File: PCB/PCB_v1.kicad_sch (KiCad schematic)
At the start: 9 parts, among them J1 Accelerometer, J2 Flysky FS2A Receiver, J3 DC-DC, J4 Battery Left, J5 Battery Right, J6 ESC Left, J7 ESC Right, J8 LED, U1 Teensy4.0

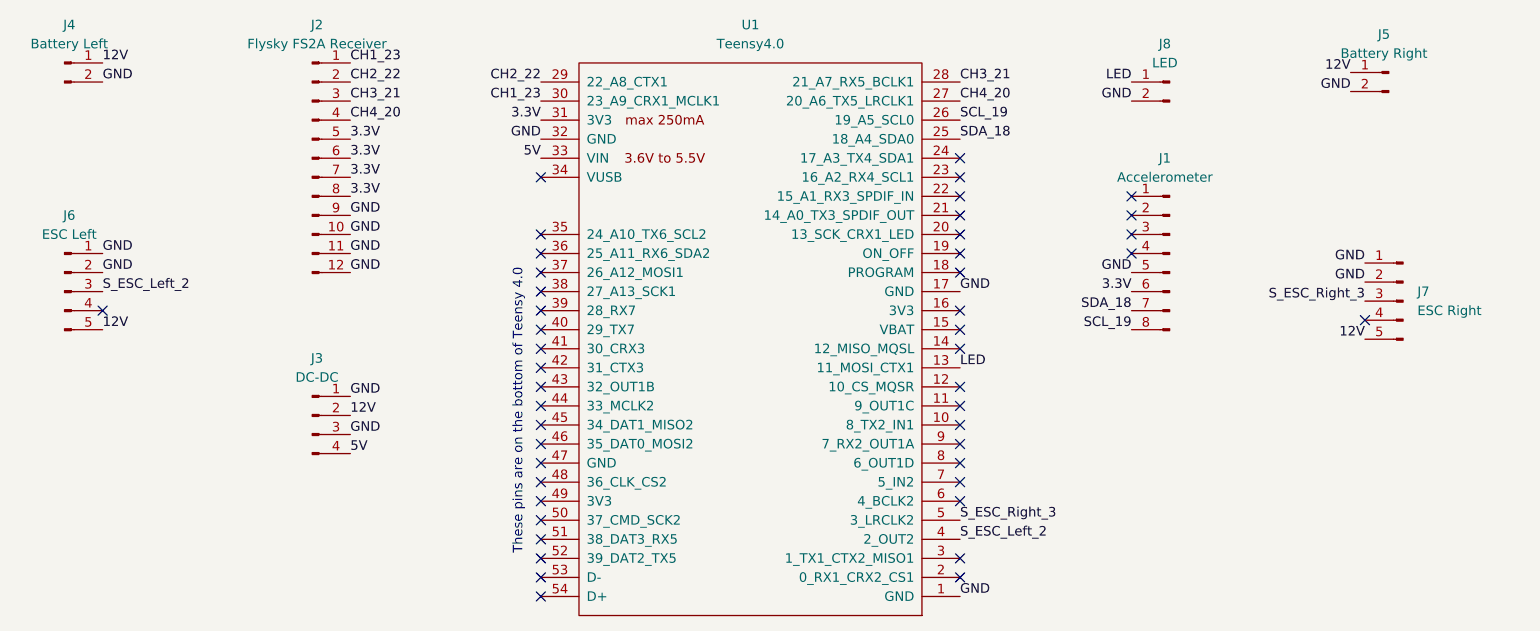
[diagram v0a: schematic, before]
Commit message: Put components onto PCB
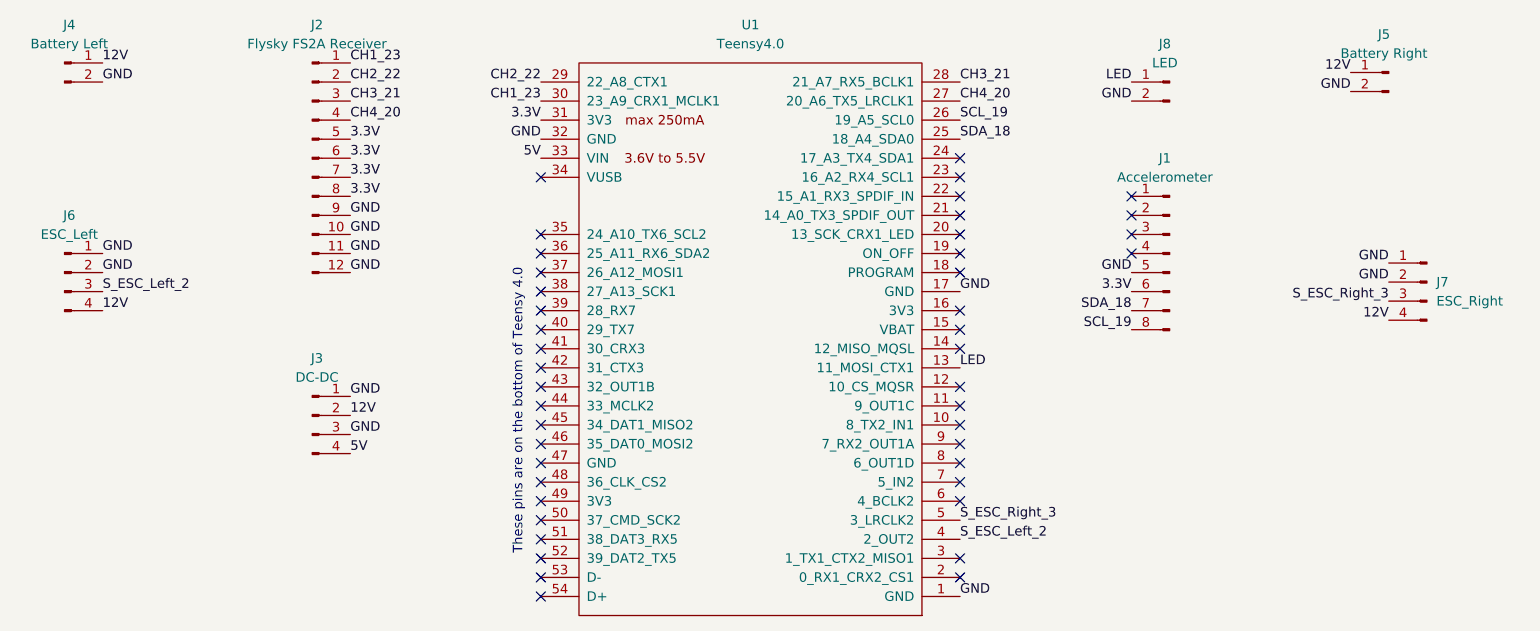
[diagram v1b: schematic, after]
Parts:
- removed J6: ESC Left, Stuffed Crust:ESC, symbol Connector:Conn_01x05_Pin
- removed J7: ESC Right, Stuffed Crust:ESC, symbol Connector:Conn_01x05_Pin
- added J6: ESC_Left, Stuffed Crust:ESC, symbol Connector:Conn_01x04_Pin
- added J7: ESC_Right, Stuffed Crust:ESC, symbol Connector:Conn_01x04_Pin
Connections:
- net 12V: now also J6.4 (Pin_4), J7.4 (Pin_4)
- net GND: now also J6.1 (Pin_1), J6.2 (Pin_2), J7.1 (Pin_1), J7.2 (Pin_2)
- net S_ESC_Left_2: now also J6.3 (Pin_3)
- net S_ESC_Right_3: now also J7.3 (Pin_3)
- no-connect marks 46 -> 44
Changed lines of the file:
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@@
-	)
-	(no_connect
-		(at 63.5 96.52)
 	)
 	(no_connect
@@
 	(no_connect
 		(at 200.66 83.82)
-	)
-	(no_connect
-		(at 231.775 97.79)
 	)
 	(no_connect
@@
 	)
 	(label "12V"
-		(at 231.775 100.33 180)
+		(at 234.95 97.79 180)
 		(effects
 			(font
@@
 	)
 	(label "GND"
-		(at 231.775 90.17 180)
+		(at 234.95 90.17 180)
 		(effects
 			(font
@@
 	)
 	(label "S_ESC_Right_3"
-		(at 231.775 95.25 180)
+		(at 234.95 95.25 180)
 		(effects
 			(font
@@
 	)
 	(label "GND"
-		(at 231.775 92.71 180)
+		(at 234.95 92.71 180)
 		(effects
 			(font
@@
 	)
 	(label "12V"
-		(at 63.5 99.06 0)
+		(at 63.5 96.52 0)
 		(effects
 			(font
@@
 			)
 			(justify left bottom)
-		)
-	)
-	(symbol
-		(lib_id "Connector:Conn_01x05_Pin")
-		(at 58.42 93.98 0)
-		(unit 1)
-		(exclude_from_sim no)
-		(in_bom yes)
-		(on_board yes)
-		(dnp no)
-		(fields_autoplaced yes)
-		(property "Reference" "J6"
-			(at 59.055 83.82 0)
-			(effects
-				(font
-					(size 1.27 1.27)
-				)
-			)
-		)
-		(property "Value" "ESC Left"
-			(at 59.055 86.36 0)
-			(effects
-				(font
-					(size 1.27 1.27)
-				)
-			)
-		)
-		(property "Footprint" "Stuffed Crust:ESC"
-			(at 58.42 93.98 0)
-			(effects
-				(font
-					(size 1.27 1.27)
-				)
-				(hide yes)
-			)
-		)
-		(property "Datasheet" "~"
-			(at 58.42 93.98 0)
-			(effects
-				(font
-					(size 1.27 1.27)
-				)
-				(hide yes)
-			)
-		)
-		(property "Description" "Generic connector, single row, 01x05, script generated"
-			(at 58.42 93.98 0)
-			(effects
-				(font
-					(size 1.27 1.27)
-				)
-				(hide yes)
-			)
-		)
-		(pin "1"
-		)
-		(pin "2"
-		)
-		(pin "3"
-		)
-		(pin "4"
-		)
-		(pin "5"
-		)
-		(instances
-			(project ""
-				(path "/be294340-84e5-4c43-afbb-c0b6a21202d8"
-					(reference "J6")
-					(unit 1)
-				)
-			)
-		)
-	)
-	(symbol
-		(lib_id "Connector:Conn_01x05_Pin")
-		(at 236.855 95.25 0)
-		(mirror y)
-		(unit 1)
-		(exclude_from_sim no)
-		(in_bom yes)
-		(on_board yes)
-		(dnp no)
-		(fields_autoplaced yes)
-		(property "Reference" "J7"
-			(at 238.76 93.9799 0)
-			(effects
-				(font
-					(size 1.27 1.27)
-				)
-				(justify right)
-			)
-		)
-		(property "Value" "ESC Right"
-			(at 238.76 96.5199 0)
-			(effects
-				(font
-					(size 1.27 1.27)
-				)
-				(justify right)
-			)
-		)
-		(property "Footprint" "Stuffed Crust:ESC"
-			(at 236.855 95.25 0)
-			(effects
-				(font
-					(size 1.27 1.27)
-				)
-				(hide yes)
-			)
-		)
-		(property "Datasheet" "~"
-			(at 236.855 95.25 0)
-			(effects
-				(font
-					(size 1.27 1.27)
-				)
-				(hide yes)
-			)
-		)
-		(property "Description" "Generic connector, single row, 01x05, script generated"
-			(at 236.855 95.25 0)
-			(effects
-				(font
-					(size 1.27 1.27)
-				)
-				(hide yes)
-			)
-		)
-		(pin "1"
-		)
-		(pin "2"
-		)
-		(pin "3"
-		)
-		(pin "4"
-		)
-		(pin "5"
-		)
-		(instances
-			(project "PCB_v1"
-				(path "/be294340-84e5-4c43-afbb-c0b6a21202d8"
-					(reference "J7")
-					(unit 1)
-				)
-			)
 		)
 	)
@@
 	)
 	(symbol
+		(lib_id "Connector:Conn_01x04_Pin")
+		(at 240.03 92.71 0)
+		(mirror y)
+		(unit 1)
+		(exclude_from_sim no)
+		(in_bom yes)
+		(on_board yes)
+		(dnp no)
+		(fields_autoplaced yes)
+		(property "Reference" "J7"
+			(at 241.3 92.7099 0)
+			(effects
+				(font
+					(size 1.27 1.27)
+				)
+				(justify right)
+			)
+		)
+		(property "Value" "ESC_Right"
+			(at 241.3 95.2499 0)
+			(effects
+				(font
+					(size 1.27 1.27)
+				)
+				(justify right)
+			)
+		)
+		(property "Footprint" "Stuffed Crust:ESC"
+			(at 240.03 92.71 0)
+			(effects
+				(font
+					(size 1.27 1.27)
+				)
+				(hide yes)
+			)
+		)
+		(property "Datasheet" "~"
+			(at 240.03 92.71 0)
+			(effects
+				(font
+					(size 1.27 1.27)
+				)
+				(hide yes)
+			)
+		)
+		(property "Description" "Generic connector, single row, 01x04, script generated"
+			(at 240.03 92.71 0)
+			(effects
+				(font
+					(size 1.27 1.27)
+				)
+				(hide yes)
+			)
+		)
+		(pin "3"
+		)
+		(pin "4"
+		)
+		(pin "1"
+		)
+		(pin "2"
+		)
+		(instances
+			(project ""
+				(path "/be294340-84e5-4c43-afbb-c0b6a21202d8"
+					(reference "J7")
+					(unit 1)
+				)
+			)
+		)
+	)
+	(symbol
 		(lib_id "Connector:Conn_01x02_Pin")
 		(at 234.95 64.77 0)
@@
 					(unit 1)
 				)
+			)
+		)
+	)
+	(symbol
+		(lib_id "Connector:Conn_01x04_Pin")
+		(at 58.42 91.44 0)
+		(unit 1)
+		(exclude_from_sim no)
+		(in_bom yes)
+		(on_board yes)
+		(dnp no)
+		(fields_autoplaced yes)
+		(property "Reference" "J6"
+			(at 59.055 83.82 0)
+			(effects
+				(font
+					(size 1.27 1.27)
+				)
+			)
+		)
+		(property "Value" "ESC_Left"
+			(at 59.055 86.36 0)
+			(effects
+				(font
+					(size 1.27 1.27)
+				)
+			)
+		)
+		(property "Footprint" "Stuffed Crust:ESC"
+			(at 58.42 91.44 0)
+			(effects
+				(font
+					(size 1.27 1.27)
+				)
+				(hide yes)
+			)
+		)
+		(property "Datasheet" "~"
+			(at 58.42 91.44 0)
+			(effects
+				(font
+					(size 1.27 1.27)
+				)
+				(hide yes)
+			)
+		)
+		(property "Description" "Generic connector, single row, 01x04, script generated"
+			(at 58.42 91.44 0)
+			(effects
+				(font
+					(size 1.27 1.27)
+				)
+				(hide yes)
+			)
+		)
+		(pin "4"
+		)
+		(pin "3"
+		)
+		(pin "2"
+		)
+		(pin "1"
+		)
+		(instances
+			(project ""
+				(path "/be294340-84e5-4c43-afbb-c0b6a21202d8"
+					(reference "J6")
+					(unit 1)
+				)

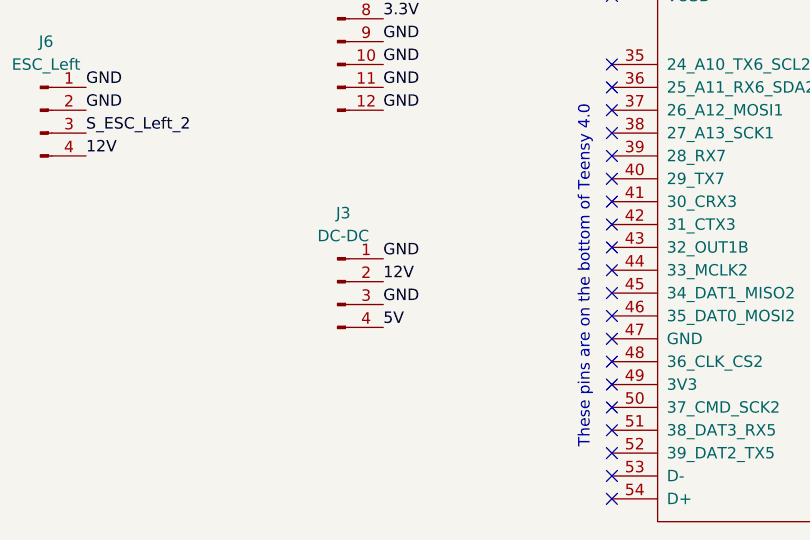
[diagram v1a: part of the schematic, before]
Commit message: Put DC_DC back to the front layer; change the PCB layout
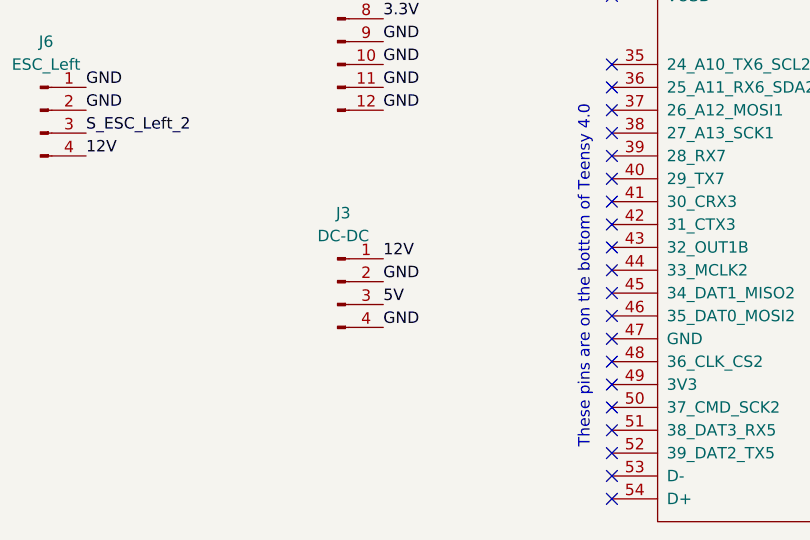
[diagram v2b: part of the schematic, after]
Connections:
- net 12V: now also J3.1 (Pin_1); no longer J3.2 (Pin_2)
- net 5V: now also J3.3 (Pin_3); no longer J3.4 (Pin_4)
- net GND: now also J3.2 (Pin_2), J3.4 (Pin_4); no longer J3.1 (Pin_1), J3.3 (Pin_3)
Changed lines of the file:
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@@
+		)
+	)
+	(label "GND"
+		(at 96.52 110.49 0)
+		(effects
+			(font
+				(size 1.27 1.27)
+			)
+			(justify left bottom)
 		)
 	)
@@
 		)
 	)
-	(label "GND"
-		(at 96.52 107.95 0)
-		(effects
-			(font
-				(size 1.27 1.27)
-			)
-			(justify left bottom)
-		)
-	)
 	(label "12V"
 		(at 229.87 64.77 180)
@@
 		)
 	)
+	(label "5V"
+		(at 96.52 113.03 0)
+		(effects
+			(font
+				(size 1.27 1.27)
+			)
+			(justify left bottom)
+		)
+	)
 	(label "S_ESC_Left_2"
 		(at 177.8 127 0)
@@
 	)
 	(label "GND"
+		(at 96.52 115.57 0)
+		(effects
+			(font
+				(size 1.27 1.27)
+			)
+			(justify left bottom)
+		)
+	)
+	(label "GND"
 		(at 121.92 73.66 180)
 		(effects
@@
 			)
 			(justify right bottom)
-		)
-	)
-	(label "12V"
-		(at 96.52 110.49 0)
-		(effects
-			(font
-				(size 1.27 1.27)
-			)
-			(justify left bottom)
 		)
 	)
@@
 		)
 	)
+	(label "12V"
+		(at 96.52 107.95 0)
+		(effects
+			(font
+				(size 1.27 1.27)
+			)
+			(justify left bottom)
+		)
+	)
 	(label "GND"
 		(at 234.95 92.71 180)
@@
 			)
 			(justify right bottom)
-		)
-	)
-	(label "GND"
-		(at 96.52 113.03 0)
-		(effects
-			(font
-				(size 1.27 1.27)
-			)
-			(justify left bottom)
 		)
 	)
@@
 		(effects
 			(font
-				(size 1.27 1.27)
-			)
-			(justify left bottom)
-		)
-	)
-	(label "5V"
-		(at 96.52 115.57 0)
-		(effects
-			(font

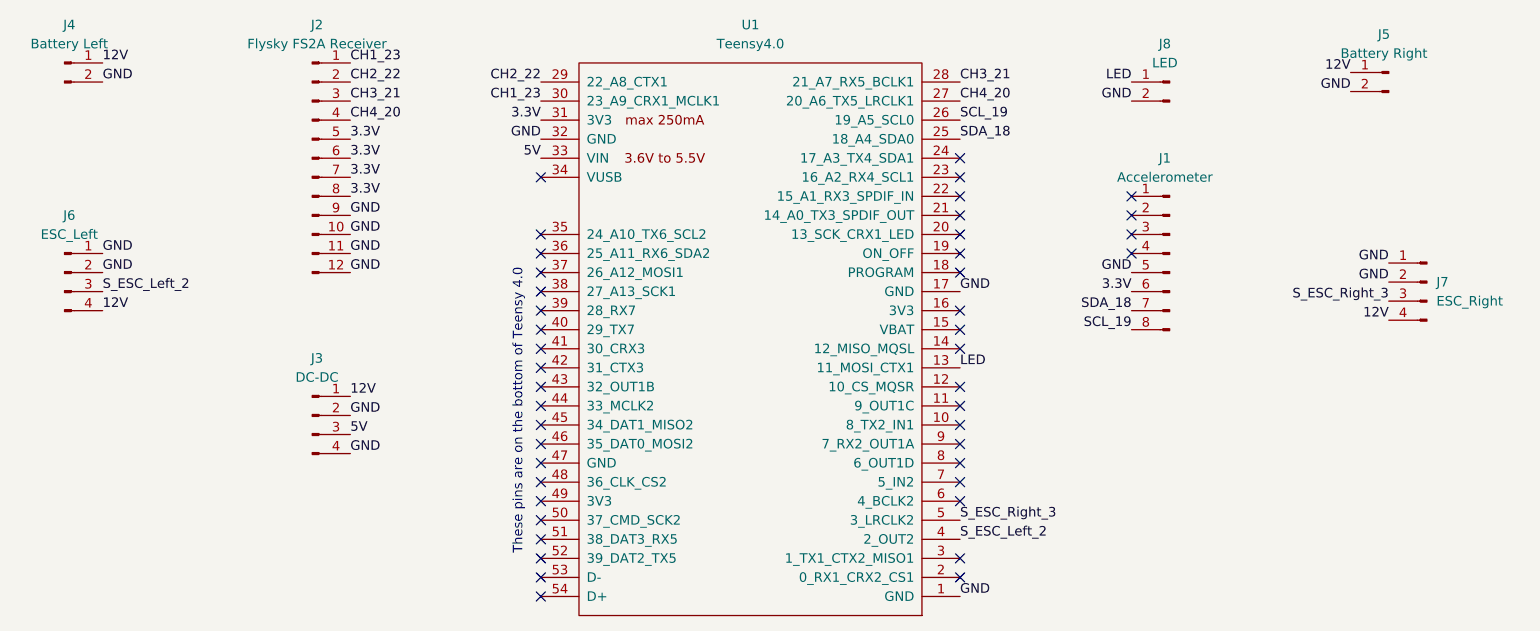
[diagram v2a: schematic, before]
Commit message: Separate GND (for signal) and GND_BT (for high current); make bigger holes for high current wires
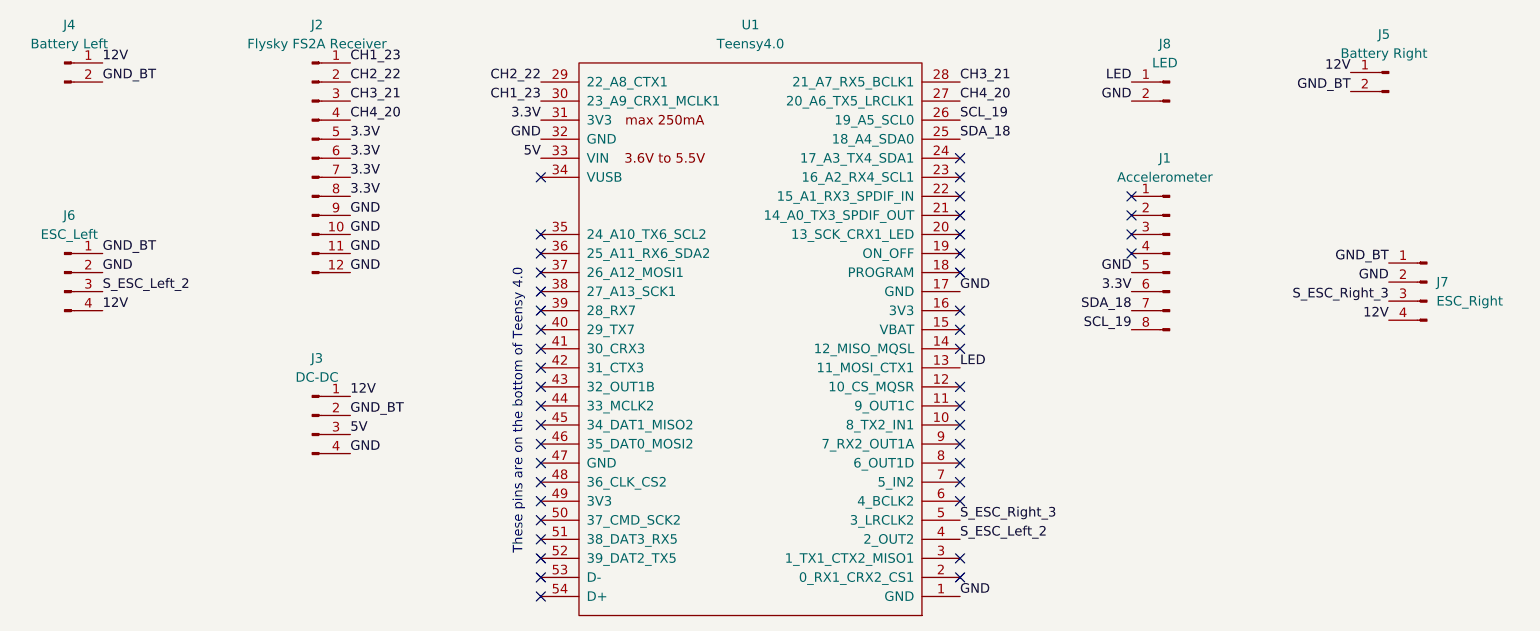
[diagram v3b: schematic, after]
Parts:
- J4, J5: footprint Stuffed Crust:Battery_or_LED -> Stuffed Crust:Battery
- J8: footprint Stuffed Crust:Battery_or_LED -> Stuffed Crust:LED
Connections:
- net GND: no longer J3.2 (Pin_2), J4.2 (Pin_2), J5.2 (Pin_2), J6.1 (Pin_1), J7.1 (Pin_1)
- new net GND_BT: J3.2 (Pin_2), J4.2 (Pin_2), J5.2 (Pin_2), J6.1 (Pin_1), J7.1 (Pin_1)
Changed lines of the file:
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@@
 		)
 	)
-	(label "GND"
+	(label "GND_BT"
 		(at 96.52 110.49 0)
 		(effects
@@
 		)
 	)
-	(label "GND"
+	(label "GND_BT"
 		(at 229.87 67.31 180)
 		(effects
@@
 		)
 	)
-	(label "GND"
+	(label "GND_BT"
 		(at 63.5 88.9 0)
 		(effects
@@
 		)
 	)
-	(label "GND"
+	(label "GND_BT"
 		(at 234.95 90.17 180)
 		(effects
@@
 		)
 	)
-	(label "GND"
+	(label "GND_BT"
 		(at 63.5 66.04 0)
 		(effects
@@
 			)
 		)
-		(property "Footprint" "Stuffed Crust:Battery_or_LED"
+		(property "Footprint" "Stuffed Crust:LED"
 			(at 205.74 66.04 0)
 			(effects
@@
 			)
 		)
-		(property "Footprint" "Stuffed Crust:Battery_or_LED"
+		(property "Footprint" "Stuffed Crust:Battery"
 			(at 58.42 63.5 0)
 			(effects
@@
 			)
 		)
-		(property "Footprint" "Stuffed Crust:Battery_or_LED"
+		(property "Footprint" "Stuffed Crust:Battery"
 			(at 234.95 64.77 0)
 			(effects
